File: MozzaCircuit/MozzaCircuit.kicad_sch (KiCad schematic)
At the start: 17 parts, among them J1 8P8C_both_sides, U1 MCP23017_ML, U2 MCP23017_ML_NoTP

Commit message: 1608 R&C
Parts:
- C1, C2: footprint 00_KeyParts:C_2012 -> 00_KeyParts:C_1608_HandSolder

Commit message: expander vias
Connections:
- net COL1: now also U1.2 (GPB5), U2.20 (GPA3); no longer U1.17 (GPA0), U2.17 (GPA0)
- net COL2: now also U1.28 (GPB3), U2.22 (GPA5); no longer U1.18 (GPA1), U2.18 (GPA1)
- net COL3: now also U1.26 (GPB1), U2.24 (GPA7); no longer U1.19 (GPA2), U2.19 (GPA2)
- net COL4: now also U1.23 (GPA6), U2.27 (GPB2); no longer U1.20 (GPA3), U2.20 (GPA3)
- net COL5: now also U1.22 (GPA5), U2.28 (GPB3); no longer U1.21 (GPA4), U2.21 (GPA4)
- net COL6: now also U1.21 (GPA4), U2.1 (GPB4); no longer U1.22 (GPA5), U2.22 (GPA5)
- net COL7: now also U1.20 (GPA3), U2.2 (GPB5); no longer U1.23 (GPA6), U2.23 (GPA6)
- net COL8: now also U1.19 (GPA2), U2.3 (GPB6); no longer U1.24 (GPA7), U2.24 (GPA7)
- net REA: now also U1.25 (GPB0), U2.25 (GPB0); no longer U1.2 (GPB5), U2.2 (GPB5)
- net REB: now also U1.24 (GPA7), U2.26 (GPB1); no longer U1.3 (GPB6), U2.3 (GPB6)
- net ROW1: now also U1.27 (GPB2), U2.23 (GPA6); no longer U1.25 (GPB0), U2.25 (GPB0)
- net ROW2: now also U1.1 (GPB4), U2.21 (GPA4); no longer U1.26 (GPB1), U2.26 (GPB1)
- net ROW3: now also U1.4 (GPB7), U2.18 (GPA1); no longer U1.27 (GPB2), U2.27 (GPB2)
- net ROW4: now also U1.3 (GPB6), U2.19 (GPA2); no longer U1.28 (GPB3), U2.28 (GPB3)
- net ROW5: now also U1.18 (GPA1), U2.4 (GPB7); no longer U1.1 (GPB4), U2.1 (GPB4)

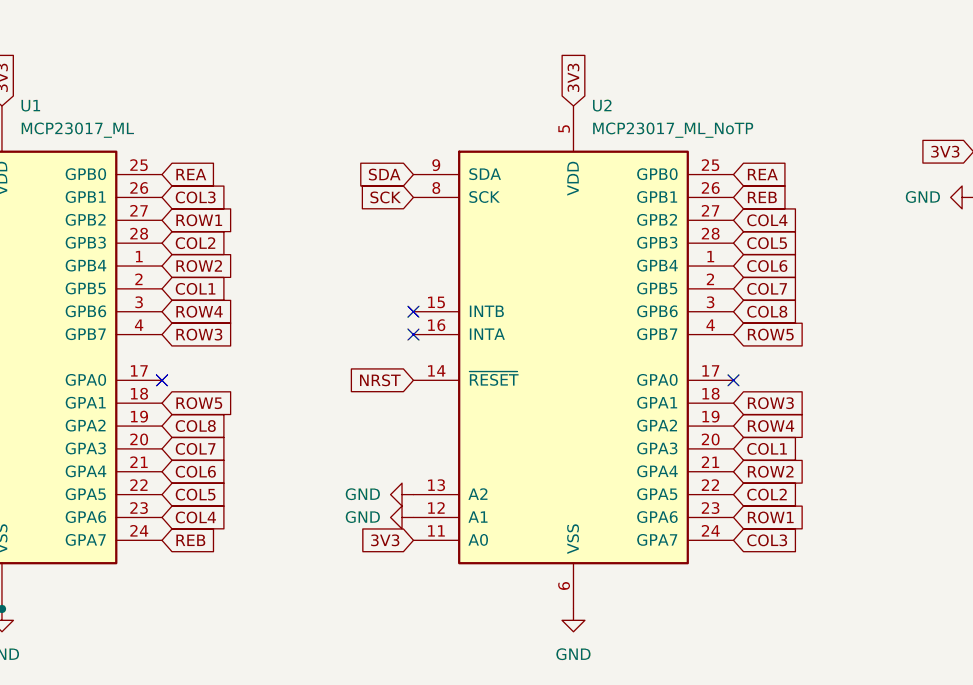
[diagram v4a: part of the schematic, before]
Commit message: drawing exp horz lines
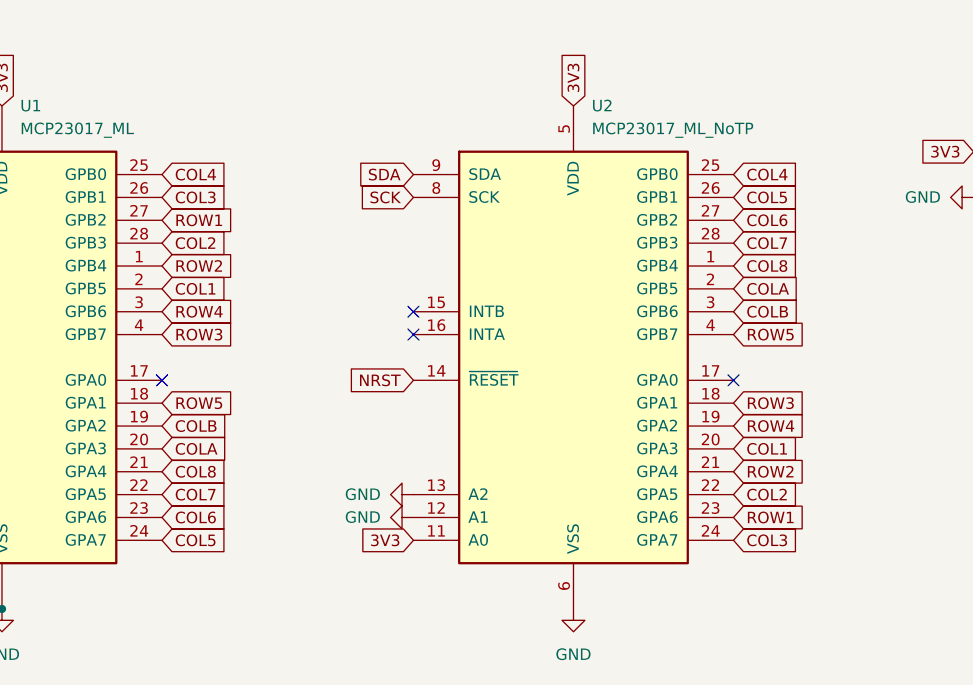
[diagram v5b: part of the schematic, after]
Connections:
- net REA is gone; now on net COL4: U1.25 (GPB0), U2.25 (GPB0)
- net REB is gone; now on net COL5: U1.24 (GPA7), U2.26 (GPB1)
- net COL4: no longer U1.23 (GPA6), U2.27 (GPB2)
- net COL5: no longer U1.22 (GPA5), U2.28 (GPB3)
- net COL6: now also U1.23 (GPA6), U2.27 (GPB2); no longer U1.21 (GPA4), U2.1 (GPB4)
- net COL7: now also U1.22 (GPA5), U2.28 (GPB3); no longer U1.20 (GPA3), U2.2 (GPB5)
- net COL8: now also U1.21 (GPA4), U2.1 (GPB4); no longer U1.19 (GPA2), U2.3 (GPB6)
- new net COLA: U1.20 (GPA3), U2.2 (GPB5)
- new net COLB: U1.19 (GPA2), U2.3 (GPB6)

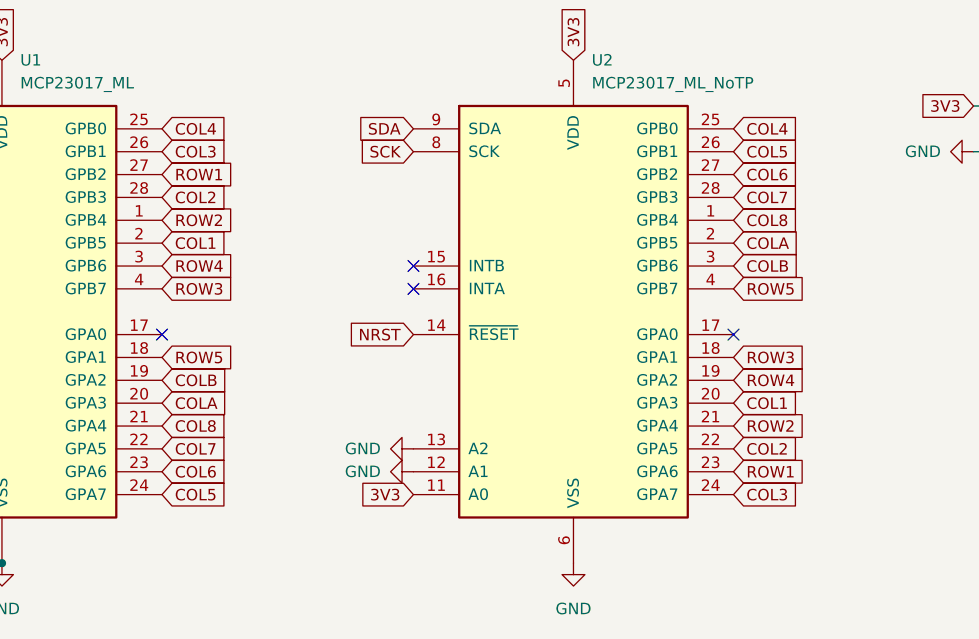
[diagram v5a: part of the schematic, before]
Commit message: led pwr line, row vert lines
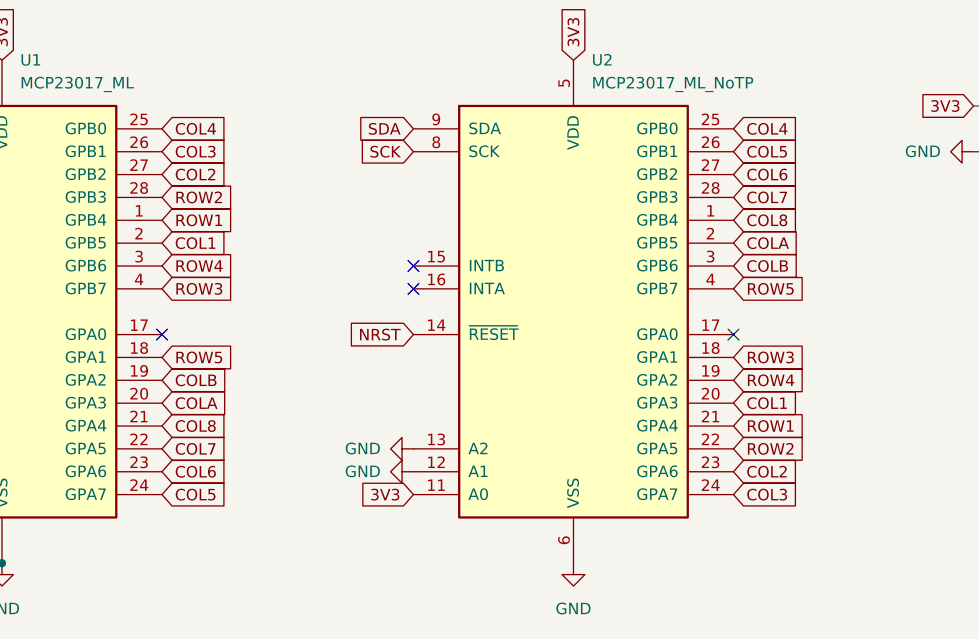
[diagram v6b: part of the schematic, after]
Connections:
- net COL2: now also U1.27 (GPB2), U2.23 (GPA6); no longer U1.28 (GPB3), U2.22 (GPA5)
- net ROW1: now also U1.1 (GPB4), U2.21 (GPA4); no longer U1.27 (GPB2), U2.23 (GPA6)
- net ROW2: now also U1.28 (GPB3), U2.22 (GPA5); no longer U1.1 (GPB4), U2.21 (GPA4)

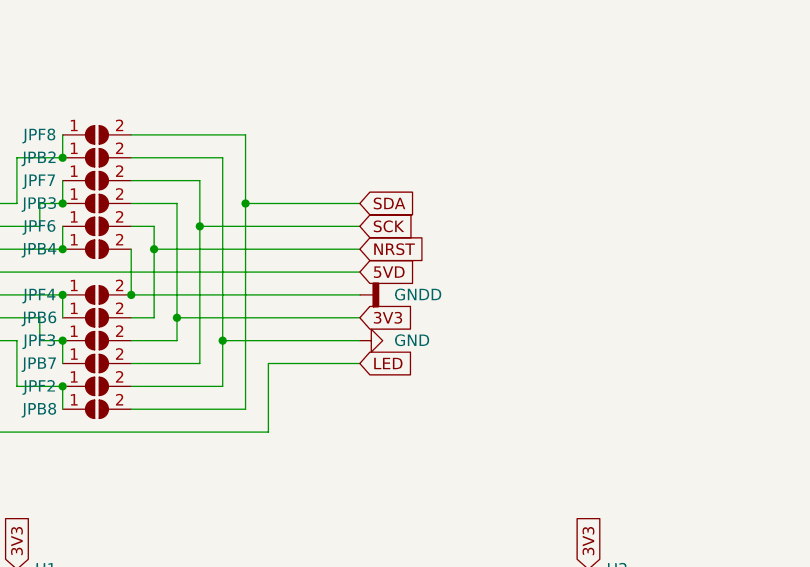
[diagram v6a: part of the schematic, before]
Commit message: wiring rj45
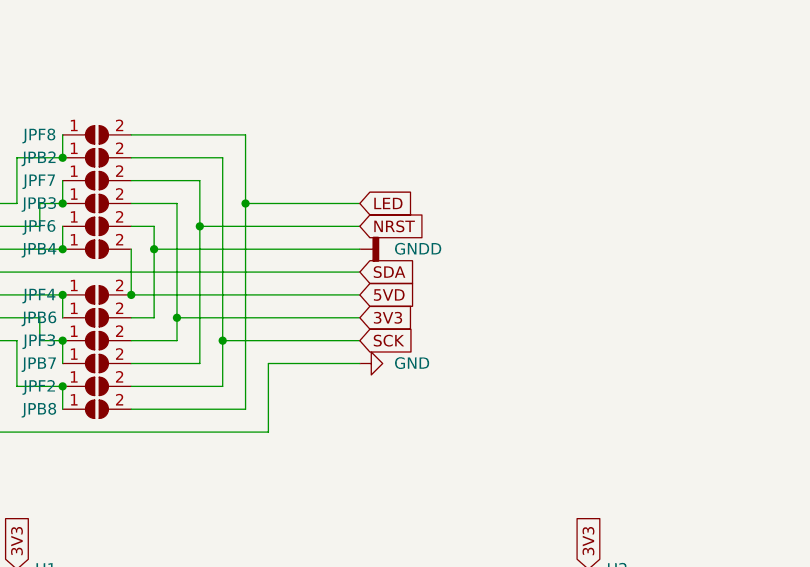
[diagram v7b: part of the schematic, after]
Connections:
- net 5VD: now also JPB4.2 (B), JPF4.2 (B); no longer J1.5
- net GND: now also J1.1, J1.9 (1); no longer JPB2.2 (B), JPF2.2 (B)
- net GNDD: now also JPB6.2 (B), JPF6.2 (B); no longer JPB4.2 (B), JPF4.2 (B)
- net LED: now also JPB8.2 (B), JPF8.2 (B); no longer J1.1, J1.9 (1)
- net NRST: now also JPB7.2 (B), JPF7.2 (B); no longer JPB6.2 (B), JPF6.2 (B)
- net SCK: now also JPB2.2 (B), JPF2.2 (B); no longer JPB7.2 (B), JPF7.2 (B)
- net SDA: now also J1.5; no longer JPB8.2 (B), JPF8.2 (B)
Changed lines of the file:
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@@
     )
   )
-  (global_label "SCK" (shape input) (at 88.9 71.12 0) (fields_autoplaced)
-    (effects (font (size 1.27 1.27)) (justify left))
-    (property "Intersheet References" "${INTERSHEET_REFS}" (id 0) (at 95.0626 71.0406 0)
+  (global_label "SCK" (shape input) (at 88.9 83.82 0) (fields_autoplaced)
+    (effects (font (size 1.27 1.27)) (justify left))
+    (property "Intersheet References" "${INTERSHEET_REFS}" (id 0) (at 95.0626 83.7406 0)
       (effects (font (size 1.27 1.27)) (justify left) hide)
     )
@@
     )
   )
-  (global_label "LED" (shape input) (at 88.9 86.36 0) (fields_autoplaced)
-    (effects (font (size 1.27 1.27)) (justify left))
-    (property "Intersheet References" "${INTERSHEET_REFS}" (id 0) (at 94.7602 86.2806 0)
+  (global_label "LED" (shape input) (at 88.9 68.58 0) (fields_autoplaced)
+    (effects (font (size 1.27 1.27)) (justify left))
+    (property "Intersheet References" "${INTERSHEET_REFS}" (id 0) (at 94.7602 68.5006 0)
       (effects (font (size 1.27 1.27)) (justify left) hide)
     )
@@
     )
   )
-  (global_label "SDA" (shape input) (at 88.9 68.58 0) (fields_autoplaced)
-    (effects (font (size 1.27 1.27)) (justify left))
-    (property "Intersheet References" "${INTERSHEET_REFS}" (id 0) (at 94.8812 68.5006 0)
+  (global_label "SDA" (shape input) (at 88.9 76.2 0) (fields_autoplaced)
+    (effects (font (size 1.27 1.27)) (justify left))
+    (property "Intersheet References" "${INTERSHEET_REFS}" (id 0) (at 94.8812 76.1206 0)
       (effects (font (size 1.27 1.27)) (justify left) hide)
     )
@@
     )
   )
-  (global_label "NRST" (shape input) (at 88.9 73.66 0) (fields_autoplaced)
-    (effects (font (size 1.27 1.27)) (justify left))
-    (property "Intersheet References" "${INTERSHEET_REFS}" (id 0) (at 96.0907 73.5806 0)
+  (global_label "NRST" (shape input) (at 88.9 71.12 0) (fields_autoplaced)
+    (effects (font (size 1.27 1.27)) (justify left))
+    (property "Intersheet References" "${INTERSHEET_REFS}" (id 0) (at 96.0907 71.0406 0)
       (effects (font (size 1.27 1.27)) (justify left) hide)
     )
@@
     )
   )
-  (global_label "5VD" (shape input) (at 88.9 76.2 0) (fields_autoplaced)
-    (effects (font (size 1.27 1.27)) (justify left))
-    (property "Intersheet References" "${INTERSHEET_REFS}" (id 0) (at 94.8812 76.1206 0)
+  (global_label "5VD" (shape input) (at 88.9 78.74 0) (fields_autoplaced)
+    (effects (font (size 1.27 1.27)) (justify left))
+    (property "Intersheet References" "${INTERSHEET_REFS}" (id 0) (at 94.8812 78.6606 0)
       (effects (font (size 1.27 1.27)) (justify left) hide)
     )
@@
     (pin "1")
   )
-  (symbol (lib_id "power:GND") (at 88.9 83.82 90) (unit 1)
-    (in_bom yes) (on_board yes) (fields_autoplaced)
-    (property "Reference" "#PWR0111" (id 0) (at 95.25 83.82 0)
-      (effects (font (size 1.27 1.27)) hide)
-    )
-    (property "Value" "GND" (id 1) (at 92.71 83.8199 90)
+  (symbol (lib_id "power:GND") (at 88.9 86.36 90) (unit 1)
+    (in_bom yes) (on_board yes) (fields_autoplaced)
+    (property "Reference" "#PWR0111" (id 0) (at 95.25 86.36 0)
+      (effects (font (size 1.27 1.27)) hide)
+    )
+    (property "Value" "GND" (id 1) (at 92.71 86.3599 90)
       (effects (font (size 1.27 1.27)) (justify right))
     )
-    (property "Footprint" "" (id 2) (at 88.9 83.82 0)
-      (effects (font (size 1.27 1.27)) hide)
-    )
-    (property "Datasheet" "" (id 3) (at 88.9 83.82 0)
+    (property "Footprint" "" (id 2) (at 88.9 86.36 0)
+      (effects (font (size 1.27 1.27)) hide)
+    )
+    (property "Datasheet" "" (id 3) (at 88.9 86.36 0)
       (effects (font (size 1.27 1.27)) hide)
     )
@@
     (pin "1")
   )
-  (symbol (lib_id "power:GNDD") (at 88.9 78.74 90) (unit 1)
-    (in_bom yes) (on_board yes)
-    (property "Reference" "#PWR0112" (id 0) (at 95.25 78.74 0)
-      (effects (font (size 1.27 1.27)) hide)
-    )
-    (property "Value" "GNDD" (id 1) (at 92.71 78.74 90)
+  (symbol (lib_id "power:GNDD") (at 88.9 73.66 90) (unit 1)
+    (in_bom yes) (on_board yes)
+    (property "Reference" "#PWR0112" (id 0) (at 95.25 73.66 0)
+      (effects (font (size 1.27 1.27)) hide)
+    )
+    (property "Value" "GNDD" (id 1) (at 92.71 73.66 90)
       (effects (font (size 1.27 1.27)) (justify right))
     )
-    (property "Footprint" "" (id 2) (at 88.9 78.74 0)
-      (effects (font (size 1.27 1.27)) hide)
-    )
-    (property "Datasheet" "" (id 3) (at 88.9 78.74 0)
-      (effects (font (size 1.27 1.27)) hide)
-    )
+    (property "Footprint" "" (id 2) (at 88.9 73.66 0)
+      (effects (font (size 1.27 1.27)) hide)
+    )
+    (property "Datasheet" "" (id 3) (at 88.9 73.66 0)
+      (effects (font (size 1.27 1.27)) hide)
+    )

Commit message: rj45 wiring
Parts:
- removed JPB3, JPB7, JPF3, JPF7: SolderJumper_2_Open, Jumper:SolderJumper-2_P1.3mm_Open_TrianglePad1.0x1.5mm, symbol Jumper:SolderJumper_2_Open
- JPB2, JPB4, JPB6, JPB8, JPF2, JPF4, JPF6, JPF8: footprint Jumper:SolderJumper-2_P1.3mm_Open_TrianglePad1.0x1.5mm -> 00_KeyParts:SolderJumper-2_P1.3mm_Open_TrianglePad1.0x1.5mm
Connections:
- net 3V3: now also JPB8.2 (B), JPF8.2 (B)
- net GND: now also JPB6.2 (B), JPF6.2 (B); no longer J1.1, J1.9 (1)
- net GNDD: now also JPB2.2 (B), JPF2.2 (B); no longer JPB6.2 (B), JPF6.2 (B)
- net LED: now also J1.1, J1.9 (1); no longer JPB8.2 (B), JPF8.2 (B)
- net NRST: now also J1.5
- net SCK_SDA: now reaches J1.7 (3)
- net SCK_SDA: now also U1.8 (SCK), U2.9 (SDA)
- net SDA_SCK: now reaches J1.3 (7)
- net SDA_SCK: now also U1.9 (SDA), U2.8 (SCK)
- removed net SCK: JPB2.2 (B), JPF2.2 (B), U1.8 (SCK), U2.8 (SCK)
- removed net SDA: J1.5, U1.9 (SDA), U2.9 (SDA)
